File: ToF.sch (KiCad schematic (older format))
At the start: 1 part, among them J5 Conn_01x05

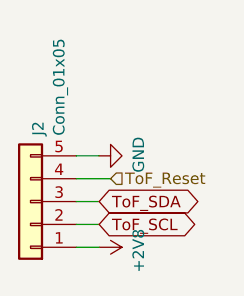
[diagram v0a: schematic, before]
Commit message: Corrected, routing redone
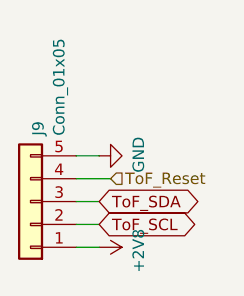
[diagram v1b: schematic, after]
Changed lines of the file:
@@
 AR Path="/5BBFB811/5BBF8577" Ref="J8"  Part="1"
 AR Path="/5BBFB816/5BBF8577" Ref="J9"  Part="1"
-F 0 "J2" V 3216 3312 50  0000 R CNN
+F 0 "J9" V 3216 3312 50  0000 R CNN
 F 1 "Conn_01x05" V 3125 3312 50  0000 R CNN
 F 2 "Connector_JST:JST_PH_B5B-PH-K_1x05_P2.00mm_Vertical" H 3250 3600 50  0001 C CNN

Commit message: Added RS refs
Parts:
- J5: RS (none) -> 820-1438
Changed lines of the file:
@@
 AR Path="/5BBFB811/5BBF8577" Ref="J8"  Part="1"
 AR Path="/5BBFB816/5BBF8577" Ref="J9"  Part="1"
-F 0 "J9" V 3216 3312 50  0000 R CNN
+F 0 "J5" V 3216 3312 50  0000 R CNN
 F 1 "Conn_01x05" V 3125 3312 50  0000 R CNN
 F 2 "Connector_JST:JST_PH_B5B-PH-K_1x05_P2.00mm_Vertical" H 3250 3600 50  0001 C CNN
 F 3 "~" H 3250 3600 50  0001 C CNN
+F 4 "820-1438" H 0   0   50  0001 C CNN "RS"
 	1    3250 3600
 	-1   0    0    1
@@
 AR Path="/5BBFB811/5BBF857E" Ref="#PWR048"  Part="1"
 AR Path="/5BBFB816/5BBF857E" Ref="#PWR050"  Part="1"
-F 0 "#PWR050" H 3550 3650 50  0001 C CNN
+F 0 "#PWR042" H 3550 3650 50  0001 C CNN
 F 1 "+2V8" H 3565 3973 50  0000 C CNN
 F 2 "" H 3550 3800 50  0001 C CNN
@@
 AR Path="/5BBFB811/5BBF8585" Ref="#PWR047"  Part="1"
 AR Path="/5BBFB816/5BBF8585" Ref="#PWR049"  Part="1"
-F 0 "#PWR049" H 3550 3150 50  0001 C CNN
+F 0 "#PWR041" H 3550 3150 50  0001 C CNN
 F 1 "GND" H 3555 3227 50  0000 C CNN
 F 2 "" H 3550 3400 50  0001 C CNN

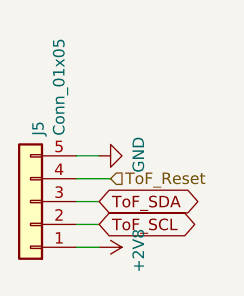
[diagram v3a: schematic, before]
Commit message: Rename phoenix phenix. Connect mounting holes to gnd.
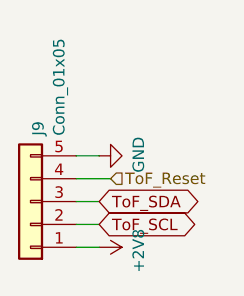
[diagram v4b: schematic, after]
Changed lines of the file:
@@
 EESchema Schematic File Version 4
+LIBS:ultraphotonicsense-elec-cache
 EELAYER 26 0
 EELAYER END
@@
 AR Path="/5BBFB811/5BBF8577" Ref="J8"  Part="1"
 AR Path="/5BBFB816/5BBF8577" Ref="J9"  Part="1"
-F 0 "J5" V 3216 3312 50  0000 R CNN
+F 0 "J9" V 3216 3312 50  0000 R CNN
 F 1 "Conn_01x05" V 3125 3312 50  0000 R CNN
 F 2 "Connector_JST:JST_PH_B5B-PH-K_1x05_P2.00mm_Vertical" H 3250 3600 50  0001 C CNN
@@
 AR Path="/5BBFB811/5BBF857E" Ref="#PWR048"  Part="1"
 AR Path="/5BBFB816/5BBF857E" Ref="#PWR050"  Part="1"
-F 0 "#PWR042" H 3550 3650 50  0001 C CNN
+F 0 "#PWR050" H 3550 3650 50  0001 C CNN
 F 1 "+2V8" H 3565 3973 50  0000 C CNN
 F 2 "" H 3550 3800 50  0001 C CNN
@@
 AR Path="/5BBFB811/5BBF8585" Ref="#PWR047"  Part="1"
 AR Path="/5BBFB816/5BBF8585" Ref="#PWR049"  Part="1"
-F 0 "#PWR041" H 3550 3150 50  0001 C CNN
+F 0 "#PWR049" H 3550 3150 50  0001 C CNN
 F 1 "GND" H 3555 3227 50  0000 C CNN
 F 2 "" H 3550 3400 50  0001 C CNN
